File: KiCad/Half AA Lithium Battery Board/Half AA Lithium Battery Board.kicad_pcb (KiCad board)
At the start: 2 copper layers, 50.8 x 30.5 mm, 5 parts, among them J1 Conn_01x04_Pin

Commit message: Update diode
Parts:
- D1: value 1N5817 -> 1N4148; footprint Diode_THT:D_DO-41_SOD81_P7.62mm_Horizontal -> Diode_THT:D_DO-35_SOD27_P7.62mm_Horizontal
- renumbered 3.6V to 3.6V1
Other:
- board text added: "JLCJLCJLCJLC"
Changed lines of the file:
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@@
       (drillshape 0)
       (scaleselection 1)
-      (outputdirectory "C:/Users/chadr/Downloads/Half AA Lithium Battery Board/Gerber/")
+      (outputdirectory "C:/Users/chadr/Downloads/KiCad Projects/Half AA Lithium Battery Board/Gerber/")
     )
   )
@@
       (net 4 "Net-(D1-A)") (pinfunction "2") (pintype "unspecified"))
   )
-  (footprint "Diode_THT:D_DO-41_SOD81_P7.62mm_Horizontal" (layer "F.Cu")
+  (footprint "Diode_THT:D_DO-35_SOD27_P7.62mm_Horizontal" (layer "F.Cu")
     (at 148.463 93.853 90)
-    (descr "Diode, DO-41_SOD81 series, Axial, Horizontal, pin pitch=7.62mm, , length*diameter=5.2*2.7mm^2, , http://www.diodes.com/_files/packages/DO-41%20(Plastic).pdf")
-    (tags "Diode DO-41_SOD81 series Axial Horizontal pin pitch 7.62mm  length 5.2mm diameter 2.7mm")
+    (descr "Diode, DO-35_SOD27 series, Axial, Horizontal, pin pitch=7.62mm, , length*diameter=4*2mm^2, , http://www.diodes.com/_files/packages/DO-35.pdf")
+    (tags "Diode DO-35_SOD27 series Axial Horizontal pin pitch 7.62mm  length 4mm diameter 2mm")
     (property "Sheetfile" "Half AA Lithium Battery Board.kicad_sch")
     (property "Sheetname" "")
@@
     (property "ki_keywords" "diode")
     (attr through_hole)
-    (fp_text reference "D1" (at 3.81 -2.47 90) (layer "F.SilkS") hide
-        (effects (font (size 1 1) (thickness 0.15)))
-    )
-    (fp_text value "1N5817" (at 3.81 2.47 90) (layer "F.Fab")
-        (effects (font (size 1 1) (thickness 0.15)))
-    )
-    (fp_text user "K" (at 0 -2.1 90) (layer "F.SilkS") hide
-        (effects (font (size 1 1) (thickness 0.15)))
-    )
-    (fp_text user "K" (at 0 -2.1 90) (layer "F.Fab")
-        (effects (font (size 1 1) (thickness 0.15)))
-    )
-    (fp_text user "${REFERENCE}" (at 4.2 0 90) (layer "F.Fab")
-        (effects (font (size 1 1) (thickness 0.15)))
-    )
-    (fp_line (start 1.09 -1.47) (end 6.53 -1.47)
+    (fp_text reference "D1" (at 3.81 -2.12 90) (layer "F.SilkS")
+        (effects (font (size 1 1) (thickness 0.15)))
+    )
+    (fp_text value "1N4148" (at 3.81 2.12 90) (layer "F.Fab")
+        (effects (font (size 1 1) (thickness 0.15)))
+    )
+    (fp_text user "K" (at 0 -1.8 90) (layer "F.SilkS") hide
+        (effects (font (size 1 1) (thickness 0.15)))
+    )
+    (fp_text user "${REFERENCE}" (at 4.11 0 90) (layer "F.Fab")
+        (effects (font (size 0.8 0.8) (thickness 0.12)))
+    )
+    (fp_text user "K" (at 0 -1.8 90) (layer "F.Fab")
+        (effects (font (size 1 1) (thickness 0.15)))
+    )
+    (fp_line (start 1.04 0) (end 1.69 0)
       (stroke (width 0.12) (type solid)) (layer "F.SilkS"))
-    (fp_line (start 1.09 -1.34) (end 1.09 -1.47)
+    (fp_line (start 1.69 -1.12) (end 1.69 1.12)
       (stroke (width 0.12) (type solid)) (layer "F.SilkS"))
-    (fp_line (start 1.09 1.34) (end 1.09 1.47)
+    (fp_line (start 1.69 1.12) (end 5.93 1.12)
       (stroke (width 0.12) (type solid)) (layer "F.SilkS"))
-    (fp_line (start 1.09 1.47) (end 6.53 1.47)
+    (fp_line (start 2.29 -1.12) (end 2.29 1.12)
       (stroke (width 0.12) (type solid)) (layer "F.SilkS"))
-    (fp_line (start 1.87 -1.47) (end 1.87 1.47)
+    (fp_line (start 2.41 -1.12) (end 2.41 1.12)
       (stroke (width 0.12) (type solid)) (layer "F.SilkS"))
-    (fp_line (start 1.99 -1.47) (end 1.99 1.47)
+    (fp_line (start 2.53 -1.12) (end 2.53 1.12)
       (stroke (width 0.12) (type solid)) (layer "F.SilkS"))
-    (fp_line (start 2.11 -1.47) (end 2.11 1.47)
+    (fp_line (start 5.93 -1.12) (end 1.69 -1.12)
       (stroke (width 0.12) (type solid)) (layer "F.SilkS"))
-    (fp_line (start 6.53 -1.47) (end 6.53 -1.34)
+    (fp_line (start 5.93 1.12) (end 5.93 -1.12)
       (stroke (width 0.12) (type solid)) (layer "F.SilkS"))
-    (fp_line (start 6.53 1.47) (end 6.53 1.34)
+    (fp_line (start 6.58 0) (end 5.93 0)
       (stroke (width 0.12) (type solid)) (layer "F.SilkS"))
-    (fp_line (start -1.35 -1.6) (end -1.35 1.6)
+    (fp_line (start -1.05 -1.25) (end -1.05 1.25)
       (stroke (width 0.05) (type solid)) (layer "F.CrtYd"))
-    (fp_line (start -1.35 1.6) (end 8.97 1.6)
+    (fp_line (start -1.05 1.25) (end 8.67 1.25)
       (stroke (width 0.05) (type solid)) (layer "F.CrtYd"))
-    (fp_line (start 8.97 -1.6) (end -1.35 -1.6)
+    (fp_line (start 8.67 -1.25) (end -1.05 -1.25)
       (stroke (width 0.05) (type solid)) (layer "F.CrtYd"))
-    (fp_line (start 8.97 1.6) (end 8.97 -1.6)
+    (fp_line (start 8.67 1.25) (end 8.67 -1.25)
       (stroke (width 0.05) (type solid)) (layer "F.CrtYd"))
-    (fp_line (start 0 0) (end 1.21 0)
+    (fp_line (start 0 0) (end 1.81 0)
       (stroke (width 0.1) (type solid)) (layer "F.Fab"))
-    (fp_line (start 1.21 -1.35) (end 1.21 1.35)
+    (fp_line (start 1.81 -1) (end 1.81 1)
       (stroke (width 0.1) (type solid)) (layer "F.Fab"))
-    (fp_line (start 1.21 1.35) (end 6.41 1.35)
+    (fp_line (start 1.81 1) (end 5.81 1)
       (stroke (width 0.1) (type solid)) (layer "F.Fab"))
-    (fp_line (start 1.89 -1.35) (end 1.89 1.35)
+    (fp_line (start 2.31 -1) (end 2.31 1)
       (stroke (width 0.1) (type solid)) (layer "F.Fab"))
-    (fp_line (start 1.99 -1.35) (end 1.99 1.35)
+    (fp_line (start 2.41 -1) (end 2.41 1)
       (stroke (width 0.1) (type solid)) (layer "F.Fab"))
-    (fp_line (start 2.09 -1.35) (end 2.09 1.35)
+    (fp_line (start 2.51 -1) (end 2.51 1)
       (stroke (width 0.1) (type solid)) (layer "F.Fab"))
-    (fp_line (start 6.41 -1.35) (end 1.21 -1.35)
+    (fp_line (start 5.81 -1) (end 1.81 -1)
       (stroke (width 0.1) (type solid)) (layer "F.Fab"))
-    (fp_line (start 6.41 1.35) (end 6.41 -1.35)
+    (fp_line (start 5.81 1) (end 5.81 -1)
       (stroke (width 0.1) (type solid)) (layer "F.Fab"))
-    (fp_line (start 7.62 0) (end 6.41 0)
+    (fp_line (start 7.62 0) (end 5.81 0)
       (stroke (width 0.1) (type solid)) (layer "F.Fab"))
-    (pad "1" thru_hole rect (at 0 0 90) (size 2.2 2.2) (drill 1.1) (layers "*.Cu" "*.Mask")
+    (pad "1" thru_hole rect (at 0 0 90) (size 1.6 1.6) (drill 0.8) (layers "*.Cu" "*.Mask")
       (net 3 "Net-(D1-K)") (pinfunction "K") (pintype "passive"))
-    (pad "2" thru_hole oval (at 7.62 0 90) (size 2.2 2.2) (drill 1.1) (layers "*.Cu" "*.Mask")
+    (pad "2" thru_hole oval (at 7.62 0 90) (size 1.6 1.6) (drill 0.8) (layers "*.Cu" "*.Mask")
       (net 4 "Net-(D1-A)") (pinfunction "A") (pintype "passive"))
-    (model "${KICAD6_3DMODEL_DIR}/Diode_THT.3dshapes/D_DO-41_SOD81_P7.62mm_Horizontal.wrl"
+    (model "${KICAD6_3DMODEL_DIR}/Diode_THT.3dshapes/D_DO-35_SOD27_P7.62mm_Horizontal.wrl"
       (offset (xyz 0 0 0))
       (scale (xyz 1 1 1))
@@
     (property "SnapEDA_Link" "https://www.snapeda.com/parts/108/Keystone+Electronics/view-part/?ref=snap")
     (attr through_hole)
-    (fp_text reference "3.6V" (at 18.4695 -6.169 90) (layer "F.SilkS")
+    (fp_text reference "3.6V1" (at 18.4695 -6.169 90) (layer "F.SilkS")
         (effects (font (size 1 1) (thickness 0.15)))
     )
@@
     (effects (font (size 3 3) (thickness 0.2) bold) (justify left bottom))
   )
+  (gr_text "JLCJLCJLCJLC" (at 166.05 85.26) (layer "F.SilkS")
+    (effects (font (size 1 1) (thickness 0.15)) (justify left bottom))
+  )
   (gr_text "Fuse:\n5mm x 20mm\n100ma" (at 178.308 98.806) (layer "F.SilkS")

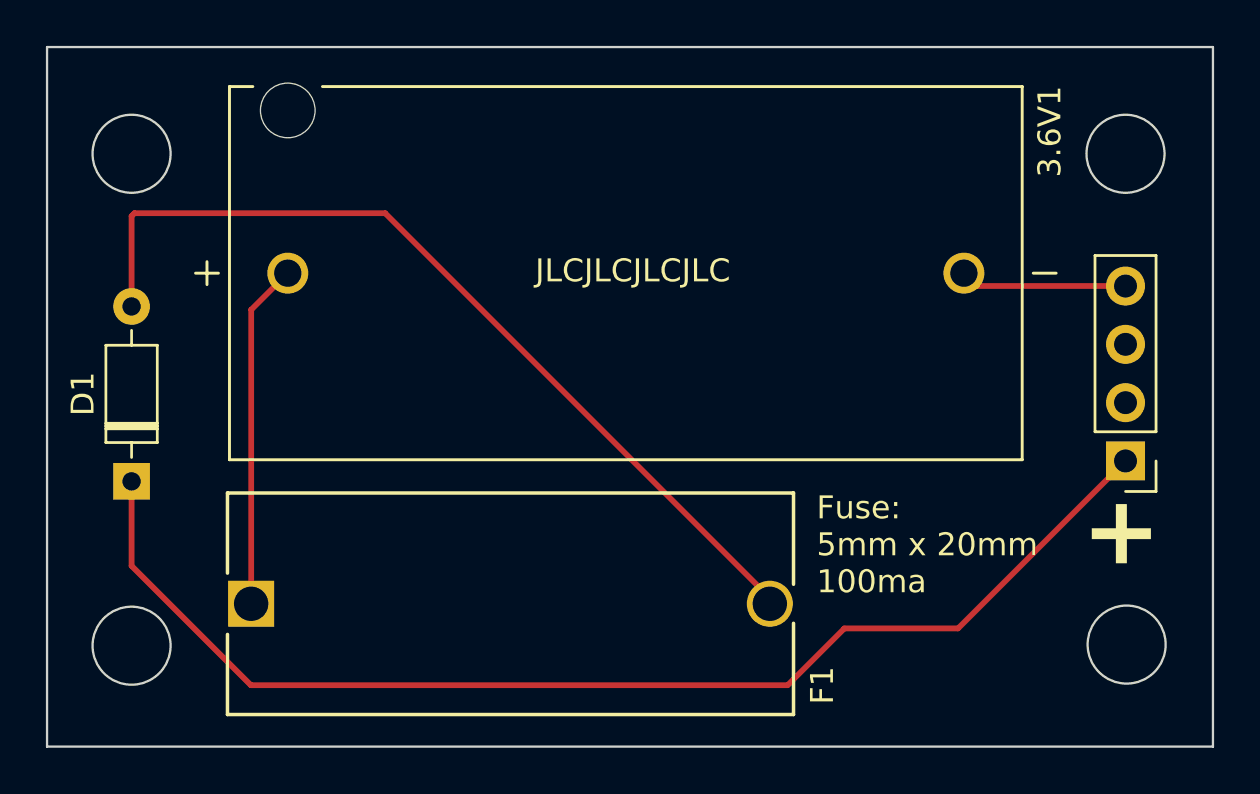
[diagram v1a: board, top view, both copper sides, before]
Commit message: add ideal diode
replace traditional diode with ideal diode chip
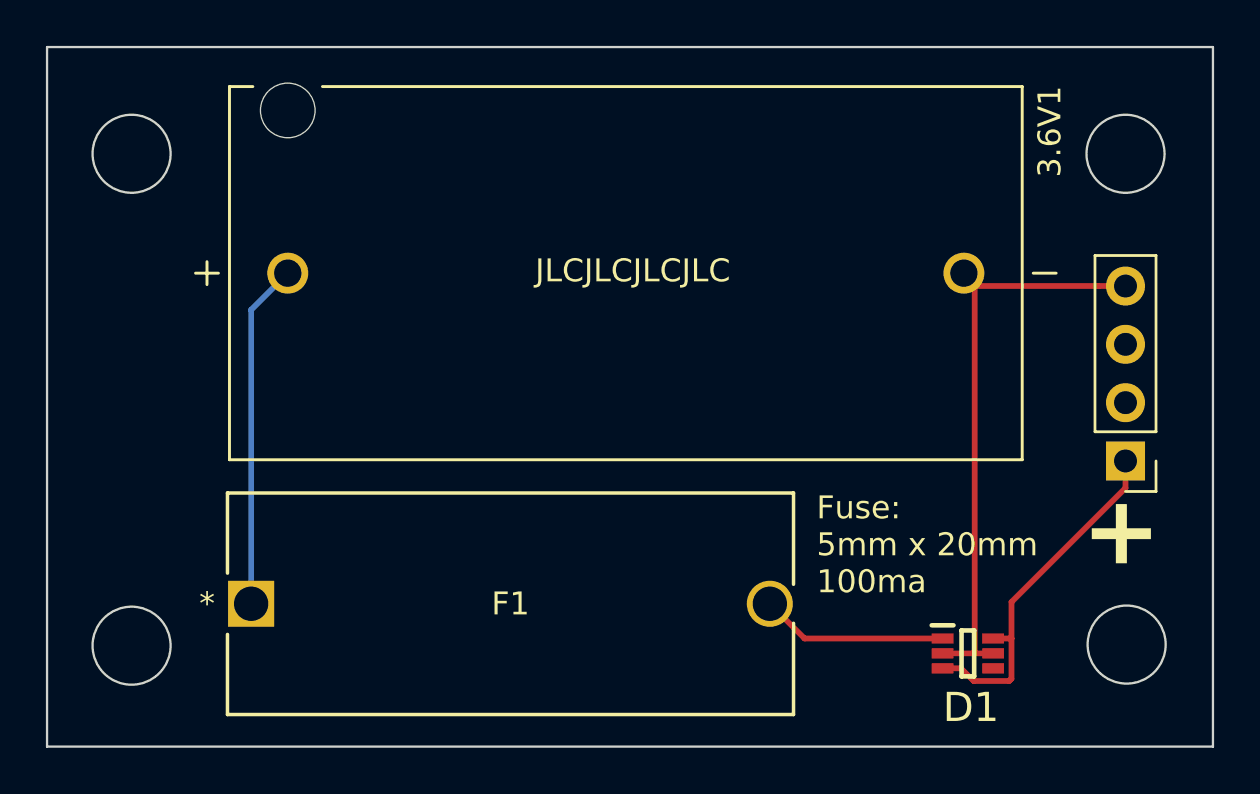
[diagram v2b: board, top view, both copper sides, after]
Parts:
- removed REF**: OSHW-Logo2_9.8x8mm_SilkScreen, Symbol:OSHW-Logo2_9.8x8mm_SilkScreen
- D1: value 1N4148 -> LM66100DCKR; footprint Diode_THT:D_DO-35_SOD27_P7.62mm_Horizontal -> LM66100DCKR:SOP65P210X110-6N
- moved D1 37.2 mm to (184.9, 101.3), turned to 0 degrees
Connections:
- 3.6V1 pad N: Net-(J1-Pin_4) -> Net-(D1-GND)
- D1 pad 1: Net-(D1-K) -> Net-(D1-VIN)
- D1 pad 2: Net-(D1-A) -> Net-(D1-GND)
- F1 pad 2: Net-(D1-A) -> Net-(D1-VIN)
- J1 pad 1: Net-(D1-K) -> Net-(D1-VOUT)
- J1 pad 4: Net-(J1-Pin_4) -> Net-(D1-GND)
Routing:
- net Net-(D1-K): track 53.2 -> 0.00 mm
- net Net-(D1-A): track 38.7 -> 0.00 mm
- net Net-(D1-GND): track 0.00 -> 25.5 mm
- net Net-(D1-VOUT): track 0.00 -> 15.6 mm
- net Net-(D1-VIN): track 0.00 -> 8.15 mm
- net Net-(J1-Pin_4): track 7.27 -> 0.00 mm
